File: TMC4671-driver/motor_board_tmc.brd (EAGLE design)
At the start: 60 x 95 mm, 135 parts, among them U1 TMC4671-ES, U10 BSC030N08NS5ATMA1, U11 BSC030N08NS5ATMA1, U12 INA28X, U13 INA28X, U14 BSC030N08NS5ATMA1, U15 BSC030N08NS5ATMA1, U16 BSC030N08NS5ATMA1, U17 BSC030N08NS5ATMA1, U18 MCP14XX, U19 BSC030N08NS5ATMA1, U20 BSC030N08NS5ATMA1, U21 BSC030N08NS5ATMA1, U22 NC7NZ17K8X-3-BUFFER, U23 NC7NZ17K8X-3-BUFFER, U3 LM5109BSD, U4 LM5109BSD, U5 LM5109BSD, U6 LM5109BSD, U7 AP3012KTR-G1, U8 LM5050Q1MK-1/NOPB, U9 BSC030N08NS5ATMA1, X1 GMSTBA4, X2 GMSTBA4, X3 2516-, Y1 ECS-327KE-TR

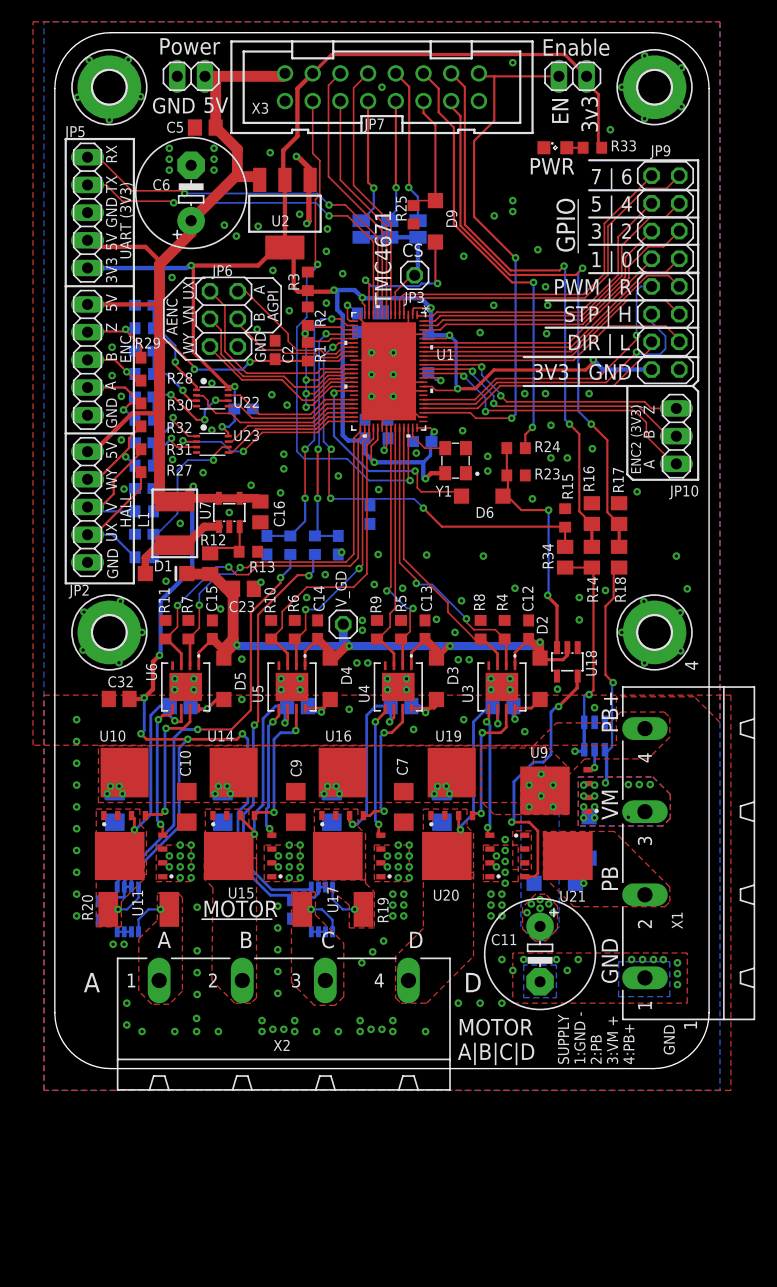
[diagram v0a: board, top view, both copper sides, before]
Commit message: Changing clearances to 8 mil and renamed shunt amps
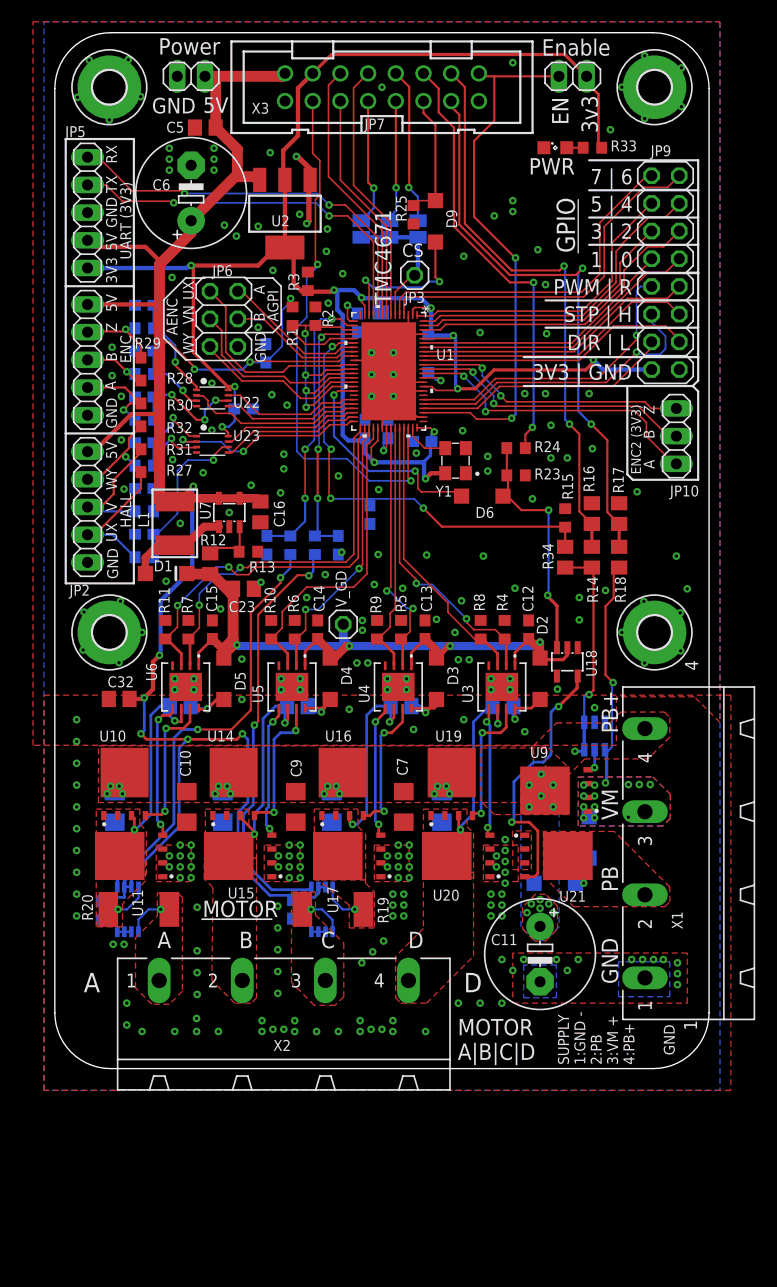
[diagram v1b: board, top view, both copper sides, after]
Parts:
- U12, U13: value INA28X -> AD841X
- moved R1 3.54 mm to (21.8, -26.0), turned to 90 degrees
- moved C2 0.90 mm to (19.4, -29.4), flipped to the bottom
- moved R2 0.70 mm to (23.9, -26.0)
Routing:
- net +5V: track 187.2 -> 195.7 mm, vias 8 -> 9
- net GND: track 41.5 -> 37.5 mm, vias 253 -> 250
- net V_ADC/2: track 33.1 -> 35.3 mm
- net REF_R: track 26.8 -> 25.9 mm

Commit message: Updated TMC4671 board to redesigned 1.2 version.
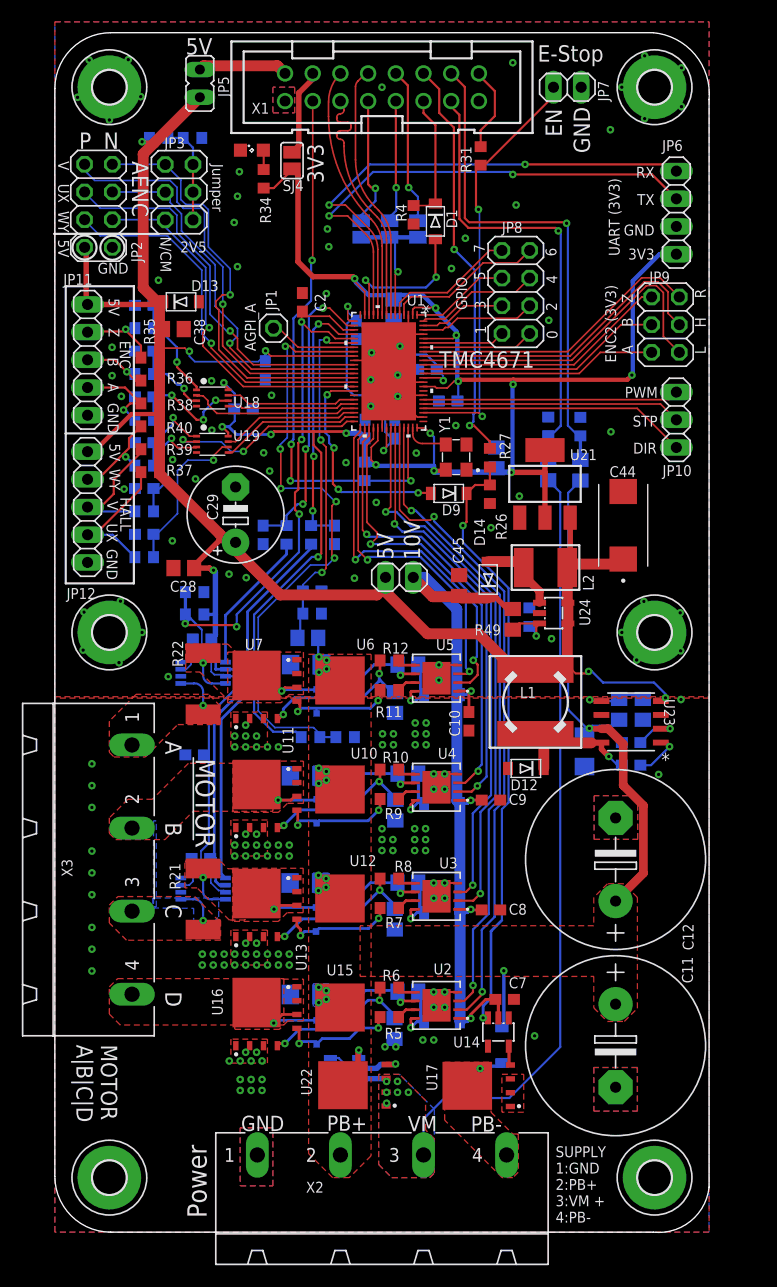
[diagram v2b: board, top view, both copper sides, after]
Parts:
- added C42: 100nF, resistor:C0603
- added C43: 1µF, resistor:C1206
- added C44: 593D476X0016D2TE3, Powermisc:CAPPM7343X310N
- added C45: 4.7µF, resistor:C0805
- added D10: BZX384-XXX, Powermisc:SOD323-R
- added D11: HV >100V, adafruit:SOD-123FL
- added D12, D14: LV low drop, adafruit:SOD-123FL
- added D13: 5.6V zener, adafruit:SOD-123FL
- added H5, H6: MOUNT-PAD-ROUND3.0, holes:3,0-PAD
- added JP11, JP12: (no value), pinhead:1X05
- added L2: 10µH, rcl:L4532P
- added R26, R50: 10k, resistor:R0603
- added R41, R42, R43, R44, R45, R46: 1.5k, resistor:R0603
- added R47: 294k, resistor:R0805
- added R48, R49: 71.5k, resistor:R0805
- added SJ4: 3.3V, jumper:SJ
- added U24: AP3012KTR-G1, Powermisc:SOT23-5L
- C10, C17, C18, C19, C7, C9: value 1µF -> 100nF; device resistor:C1206 -> resistor:C0603
- C11: value 100µF+ -> 680µF; device resistor:E5-10,5 -> resistor:E7,5-16
- C12: value 100nF -> 680µF; device resistor:C0603 -> resistor:E7,5-16
- C13, C14, C15: value 100nF -> 1µF; device resistor:C0603 -> resistor:C1206
- C16: value 4.7µF -> 1µF; device resistor:C0805 -> resistor:C1206
- C20: value 1µF -> 4.7µF; device resistor:C1206 -> resistor:C0805
- C21, C22, C24: device resistor:C0603 -> resistor:C0805
- C23: value 4.7µF -> 100nF
- C25, C30, C31: value 100nF -> 1n
- C26, C27: device resistor:C0805 -> resistor:C0603
- C28: value 100nF -> 4.7µF
- C29: value 100nF -> (none); device resistor:C0805 -> resistor:E5-8,5
- C32: value 4.7µF -> 100p; device resistor:C0805 -> resistor:C0603
- C33, C35, C37: value 2.2n -> 1n
- C34, C36: value 2.2n -> 100p
- C38, C40: value 2.2n -> 4.7µF; device resistor:C0603 -> resistor:C0805
- C39: value 2.2n -> 100nF; device resistor:C0603 -> resistor:C0805
- C41: value 2.2n -> 100nF
- C5, C8: value 4.7µF -> 100nF; device resistor:C0805 -> resistor:C0603
- C6: value 60µF+ -> 100nF; device resistor:E5-10,5 -> resistor:C0603
- D1, D2, D3, D4, D5: device diode:SOD123 -> adafruit:SOD-123FL
- D6: value LV low drop -> BZX384-XXX; device diode:SOD123 -> Powermisc:SOD323-R
- D7, D8: value HV >100V -> BZX384-XXX; device diode:SOD123 -> Powermisc:SOD323-R
- D9: value HV >100V -> LV low drop; device diode:SOD123 -> adafruit:SOD-123FL
- JP1: device pinhead:1X05 -> pinhead:1X01
- JP2: device pinhead:1X05 -> pinhead:2X04
- JP3: device pinhead:1X01 -> pinhead:2X03
- JP4: device pinhead:1X01 -> pinhead:1X02
- JP5: value (none) -> 5V; device pinhead:1X05 -> jumper:JP1
- JP6: device pinhead:2X03 -> pinhead:1X04
- JP8: device pinhead:1X02 -> pinhead:2X04
- JP9: device pinhead:2X08 -> pinhead:2X03
- L1: value 10µH -> 220µH; device rcl:L4532P -> Powermisc:8MMINDUCTOR
- LED1: value (none) -> Green
- R10, R11, R5, R6, R7, R8, R9: value 10k -> 2.2
- R12: value 33k -> 2.2; device resistor:R0805 -> resistor:R0603
- R13: value 4.7k -> 71.5k; device resistor:R0603 -> resistor:R0805
- R14: value 976k -> 1.5k; device resistor:R0805 -> resistor:R0603
- R15: value 4.7k -> 294k; device resistor:R0603 -> resistor:R0805
- R16: value 33k -> 10k; device resistor:R0805 -> resistor:R0603
- R17: value 976k -> 33k
- R18: value 33k -> 294k
- R19: value 1.5m -> 10k; device resistor:R2512 -> resistor:R0603
- R20: value 1.5m -> 33k; device resistor:R2512 -> resistor:R0805
- R21, R22: value 1k -> 1.5m; device resistor:R0603 -> resistor:R2512
- R23: value 10k -> 1.5k
- R24: value 1k -> 1.5k
- R25: value 10k -> 33k; device resistor:R0603 -> resistor:R0805
- R27, R30, R31: value 4.7k -> 1.5k
- R28: value 4.7k -> 33k; device resistor:R0603 -> resistor:R0805
- R29: value 4.7k -> 22k thermistor
- R32: value 4.7k -> 10k
- R33: value 330 -> 10k
- R34: value 360k -> 330; device resistor:R0805 -> resistor:R0603
- R35, R36, R37, R38, R39, R40: value 1k -> 4.7k
- U1: value TMC4671-ES -> TMC4671
- U12, U13: value AD841X -> BSC030N08NS5ATMA1; device Powermisc:MSOP8 -> OHSC_Power:MOSFET_BSC093N04LSGATMA1
- U14: value BSC030N08NS5ATMA1 -> MCP14XX; device OHSC_Power:MOSFET_BSC093N04LSGATMA1 -> Powermisc:SOT23-5L
- U18: value MCP14XX -> NC7NZ17K8X-3-BUFFER; device Powermisc:SOT23-5L -> Powermisc:VFSOP-8
- U19: value BSC030N08NS5ATMA1 -> NC7NZ17K8X-3-BUFFER; device OHSC_Power:MOSFET_BSC093N04LSGATMA1 -> Powermisc:VFSOP-8
- U2: value (none) -> LM5109BSD; device SparkFun-IC-Power:SOT223 -> Powermisc:SDC08A
- U20: value BSC030N08NS5ATMA1 -> LM74700-Q1; device OHSC_Power:MOSFET_BSC093N04LSGATMA1 -> OHSC_Power:SOT23-6
- U21: value BSC030N08NS5ATMA1 -> (none); device OHSC_Power:MOSFET_BSC093N04LSGATMA1 -> SparkFun-IC-Power:SOT223
- U22: value NC7NZ17K8X-3-BUFFER -> BSC030N08NS5ATMA1; device Powermisc:VFSOP-8 -> OHSC_Power:MOSFET_BSC093N04LSGATMA1
- U23: value NC7NZ17K8X-3-BUFFER -> MAX5033BASA+T; device Powermisc:VFSOP-8 -> Powermisc:21-0041B_8_MXM
- U6: value LM5109BSD -> BSC030N08NS5ATMA1; device Powermisc:SDC08A -> OHSC_Power:MOSFET_BSC093N04LSGATMA1
- U7: value AP3012KTR-G1 -> BSC030N08NS5ATMA1; device Powermisc:SOT23-5L -> OHSC_Power:MOSFET_BSC093N04LSGATMA1
- U8: value LM5050Q1MK-1/NOPB -> AD841X; device OHSC_Power:SOT95P280X110-6N -> Powermisc:MSOP8
- U9: value BSC030N08NS5ATMA1 -> AD841X; device OHSC_Power:MOSFET_BSC093N04LSGATMA1 -> Powermisc:MSOP8
- X1: value GMSTBA4 -> 2516-; device con-phoenix-762:GMSTBA4 -> con-3m:PAK100/2500-16
- X3: value 2516- -> GMSTBA4; device con-3m:PAK100/2500-16 -> con-phoenix-762:GMSTBA4
- Y1: value ECS-327KE-TR -> 25MHz
- moved H1 100.0 mm to (55.0, -105.0)
- moved X3 77.0 mm to (2.00, -76.8), turned to 270 degrees
- moved X1 76.1 mm to (30.0, -5.00), turned to 0 degrees
- moved U2 73.9 mm to (35.0, -89.2), turned to 90 degrees
- moved C39 71.1 mm to (26.2, -98.0)
- moved H2 70.7 mm to (5.00, -105.0)
- moved R25 64.6 mm to (31.2, -81.3), flipped to the bottom
- moved U22 64.4 mm to (27.5, -96.5), turned to 90 degrees
- moved R28 63.5 mm to (31.1, -91.3), flipped to the bottom, turned to 90 degrees
- moved C21 60.3 mm to (32.4, -88.0)
- moved C8 54.8 mm to (40.0, -80.5), flipped to the top, turned to 180 degrees
- moved C41 54.8 mm to (52.9, -65.1)
- moved H3 50.0 mm to (55.0, -5.00)
- moved H4 50.0 mm to (55.0, -55.0)
- moved R19 48.5 mm to (45.2, -36.1), flipped to the bottom, turned to 270 degrees
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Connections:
- removed net N$14: C28.1, D4.C, U5.8
- removed net N$26: C26.1, D2.C, U3.8
- removed net VCORE1: C3.2, U1.15
- removed net VCORE2: C1.2, U1.45
- removed net VCORE3: C4.2, U1.63
- removed net V_ADC/2: R1.1, R2.2, U1.17, U1.19, U1.26, U1.28, U1.30
- new net AENC_UX_N: JP2.5, JP3.3, U1.26
- new net AENC_VN_N: JP2.7, JP3.1, U1.28
- new net AENC_WY_N: JP2.3, JP3.5, U1.30
- new net INPUT_GATE: U20.5, U22.4
- new net N$16: C42.2, D12.C, L1.1, U23.8
- new net N$17: R31.2, X1.16
- new net N$19: C42.1, U23.1
- new net N$20: SJ4.1, X1.4
- new net N$21: R47.1, R48.1, U23.5
- new net N$23: JP5.1, X1.2
- new net N$24: C39.1, U20.1
- new net N$25: C41.2, U23.2
- new net N$27: R11.2, U5.7
- new net N$28: C23.1, D4.C, U4.8
- new net N$29: R10.2, U4.5
- new net N$30: R9.2, U4.7
- new net N$31: C21.1, D2.C, U2.8
- new net N$32: R6.2, U2.5
- new net N$33: R5.2, U2.7
- new net N$34: C22.1, D3.C, U3.8
- new net N$35: R8.2, U3.5
- new net N$36: R7.2, U3.7
- new net VCORE: C3.2, C5.2, C6.2, U1.15, U1.45, U1.63
- new net V_SENSE/2: C1.2, C2.2, R1.1, R2.2, U1.17, U1.19, U8.3, U8.7, U9.3, U9.7
- net +3V3: now also C17.1, C18.1, C19.1, C20.1, C40.1, JP6.4, R29.2, R34.2, SJ4.2, U18.P$8, U19.P$8, U21.2, U21.4; no longer C21.1, C22.1, C24.1, C25.1, C8.1, JP5.5, JP7.2, JP9.2, R33.2, U2.2, U2.4, U22.P$8, U23.P$8, X3.4
- net +5V: now also C26.1, C27.1, C28.1, C29.+, C38.1, C4.2, C44.1, D13.C, JP11.1, JP12.1, JP2.2, JP4.2, JP5.2, L1.2, L2.1, R35.2, R36.2, R37.2, R38.2, R39.2, R40.2, U21.3, U23.4, U24.4, U24.5, U8.6, U9.6; no longer C16.1, C2.2, C30.1, C31.1, C32.1, C5.1, C6.+, JP1.1, JP2.1, JP5.4, JP8.1, L1.1, R27.2, R28.2, R29.2, R30.2, R31.2, U12.6, U12.7, U13.6, U13.7, U2.3, U7.4, U7.5, X3.2
- net AENC_UX: now also JP2.6; no longer JP6.1
- net AENC_VN: now also JP2.8; no longer JP6.3
- net AENC_WY: now also JP2.4; no longer JP6.5
- net AGPI_A: now also JP1.1; no longer JP6.2
- net AGPI_B: now also R29.1, R30.2; no longer JP6.4
- net BRAKE_CTRL: now also D9.C, R26.2, R27.2, U14.3; no longer D6.C, R23.2, R24.2, U18.3
- net BRAKE_CTRL_EXT: now also R27.1, X1.12; no longer R24.1, X3.12
- net BRAKE_CTRL_TMC: now also D9.A; no longer D6.A
- net BRAKE_GATE: now also U14.5, U17.4; no longer U18.5, U21.4
- net CS1: now also X1.7; no longer X3.7
- net CS2: now also X1.9; no longer X3.9
- net CS3: now also X1.10; no longer X3.10
- net CS_TMC: no longer JP3.1
- net C_HS_A: now also U5.2; no longer R7.2, U6.2
- net C_HS_B: now also U4.2; no longer R6.2, U5.2
- net C_HS_C: now also U3.2; no longer R5.2, U4.2
- net C_HS_D: now also U2.2; no longer R4.2, U3.2
- net C_LS_A: now also U5.3; no longer R11.2, U6.3
- net C_LS_B: now also U4.3; no longer R10.2, U5.3
- net C_LS_C: now also U3.3; no longer R9.2, U4.3
- net C_LS_D: now also U2.3; no longer R8.2, U3.3
- net DIR: now also JP10.3; no longer JP9.4
- net ENABLE: now also JP7.2, R31.1; no longer JP7.1, X3.16
- net ENC2_A: now also JP9.2; no longer JP10.1
- net ENC2_B: now also JP9.4; no longer JP10.2
- net ENC2_Z: now also JP9.6; no longer JP10.3
- net ENC_A: now also U18.P$2; no longer U22.P$2
- net ENC_A_5V: now also C36.2, R46.1, U18.P$6; no longer C41.2, R40.1, U22.P$6
- net ENC_B: now also U18.P$5; no longer U22.P$5
- net ENC_B_5V: now also C34.2, R45.1, U18.P$3; no longer C39.2, R39.1, U22.P$3
- net ENC_Z: now also U18.P$7; no longer U22.P$7
- net ENC_Z_5V: now also C32.2, R44.1, U18.P$1; no longer C40.2, R38.1, U22.P$1
- net FLAG: now also D1.C, R4.2, X1.11; no longer D9.C, R25.2, X3.11
- net GND: now also C10.1, C12.-, C13.2, C14.2, C15.2, C26.2, C27.2, C28.2, C29.-, C30.1, C31.1, C32.1, C33.1, C38.2, C40.2, C43.1, C44.2, C45.2, C5.1, C6.1, C7.1, C8.1, C9.1, D12.A, D13.A, H5.B3,0, H6.B3,0, JP11.5, JP12.5, JP2.1, JP6.3, JP7.1, R14.1, R17.1, R19.1, R20.1, R26.1, R28.1, R30.1, R33.1, R48.2, R50.1, U13.1, U14.1, U14.4, U16.1, U16.2, U16.3, U18.P$4, U19.P$4, U2.4, U2.9, U23.3, U23.6, U24.2, U7.1, U7.3, U9.2, X2.1; no longer C10.2, C12.1, C13.1, C14.1, C15.1, C21.2, C22.2, C23.2, C24.2, C30.2, C31.2, C32.2, C33.2, C38.1, C39.1, C40.1, C5.2, C6.-, C7.2, C8.2, C9.2, D8.A, JP1.5, JP2.5, JP5.3, JP6.6, JP8.2, JP9.1, R10.1, R11.1, R13.1, R15.1, R18.1, R23.1, R5.1, R6.1, R7.1, R8.1, R9.1, U12.2, U12.3, U12.4, U13.4, U15.1, U15.2, U15.3, U18.1, U18.4, U2.1, U20.1, U20.3, U21.2, U21.3, U22.P$4, U23.P$4, U6.4, U6.9, U8.3, X3.1
- net GPIO0: now also JP8.1; no longer JP9.9
- net GPIO1: now also JP8.2; no longer JP9.10
- net GPIO2: now also JP8.3; no longer JP9.11
- net GPIO3: now also JP8.4; no longer JP9.12
- net GPIO4: now also JP8.5; no longer JP9.13
- net GPIO5: now also JP8.6; no longer JP9.14
- net GPIO6: now also JP8.7; no longer JP9.15
- net GPIO7: now also JP8.8; no longer JP9.16
- net G_HS_A: now also D6.C, R11.1, U6.4; no longer U10.4, U6.7
- net G_HS_B: now also D7.C, R9.1, U10.4; no longer U14.4, U5.7
- net G_HS_C: now also D8.C, R7.1, U12.4; no longer U16.4, U4.7
- net G_HS_D: now also D10.C, R5.1, U15.4; no longer U19.4, U3.7
- net G_LS_A: now also R12.1, R17.2, U7.4; no longer U11.4, U6.5
- net G_LS_B: now also R10.1, R20.2, U11.4; no longer U15.4, U5.5
- net G_LS_C: now also R25.2, R8.1, U13.4; no longer U17.4, U4.5
- net G_LS_D: now also R28.2, R6.1, U16.4; no longer U20.4, U3.5
- net HALL_UX: now also U19.P$2; no longer U23.P$2
- net HALL_UX_5V: now also C33.2, R41.1, U19.P$6; no longer C37.2, R35.1, U23.P$6
- net HALL_V: now also U19.P$5; no longer U23.P$5
- net HALL_V_5V: now also C35.2, R42.1, U19.P$3; no longer C36.2, R36.1, U23.P$3
- net HALL_WY: now also U19.P$7; no longer U23.P$7
- net HALL_WY_5V: now also C37.2, R43.1, U19.P$1; no longer C38.2, R37.1, U23.P$1
- net MISO: now also X1.6; no longer X3.6
- net MOSI: now also X1.5; no longer X3.5
- net MOT_A: now also C24.2, D6.A, R22.2, U5.6, U6.1, U6.2, U6.3, U7.5, U8.8; no longer C29.2, R20.2, U10.1, U10.2, U10.3, U11.5, U12.8, U6.6
- net MOT_A_OUT: now also R22.1, U8.1, X3.1; no longer R20.1, U12.1, X2.1
- net MOT_B: now also C23.2, D7.A, U10.1, U10.2, U10.3, U11.5, U4.6, X3.2; no longer C28.2, U14.1, U14.2, U14.3, U15.5, U5.6, X2.2
- net MOT_C: now also C22.2, D8.A, R21.2, U12.1, U12.2, U12.3, U13.5, U3.6, U9.8; no longer C27.2, R19.2, U13.8, U16.1, U16.2, U16.3, U17.5, U4.6
- net MOT_C_OUT: now also R21.1, U9.1, X3.3; no longer R19.1, U13.1, X2.3
- net MOT_D: now also C21.2, D10.A, U15.1, U15.2, U15.3, U16.5, U2.6, X3.4; no longer C26.2, U19.1, U19.2, U19.3, U20.5, U3.6, X2.4
- net N$1: now also JP12.4, R37.1, R41.2; no longer JP2.4, R27.1, R35.2
- net N$10: now also R24.2, U9.5; no longer R22.2, U13.5
- net N$11: now also JP11.2, R35.1, R44.2; no longer JP1.2, R29.1, R38.2
- net N$12: now also D14.A, L2.2, U24.1; no longer D1.A, L1.2, U7.1
- net N$13: now also R12.2, U5.5; no longer U8.5, U9.4
- net N$15: now also JP12.2, R40.1, R43.2; no longer JP2.2, R32.1, R37.2
- net N$18: now also C24.1, U5.8; no longer C29.1, U6.8
- net N$2: now also X1.15; no longer X3.15
- net N$22: now also JP3.2, JP3.4, JP3.6, R32.1, R33.2; no longer C27.1, D3.C, U4.8
- net N$3: now also JP12.3, R39.1, R42.2; no longer JP2.3, R31.1, R36.2
- net N$4: now also D1.A; no longer D9.A
- net N$5: now also R49.1, R50.2, U24.3; no longer R12.1, R13.2, U7.3
- net N$6: now also R23.2, U8.5; no longer R21.2, U12.5
- net N$7: now also JP11.4, R38.1, R46.2; no longer JP1.4, R30.1, R40.2
- net N$8: now also R34.1; no longer R33.1
- net N$9: now also JP11.3, R36.1, R45.2; no longer JP1.3, R28.1, R39.2
- net PWM_I: now also JP10.1; no longer JP9.8
- net REF_H: now also JP9.3; no longer JP9.5
- net REF_L: now also JP9.1; no longer JP9.3
- net REF_R: now also JP9.5; no longer JP9.7
- net RESET: now also X1.3; no longer X3.3
- net RES_FET: now also D11.A, U17.5, X2.4; no longer D7.A, U21.5, X1.2
- net SCK: now also X1.8; no longer X3.8
- net SENSE_A: now also C30.2, R23.1; no longer C34.2, R21.1
- net SENSE_C: now also C31.2, R24.1; no longer C35.2, R22.1
- net STEP: now also JP10.2; no longer JP9.6
- net UART_RX: now also JP6.1; no longer JP5.1
- net UART_TX: now also JP6.2; no longer JP5.2
- net V+: now also C12.+, C13.1, C14.1, C15.1, C16.1, C43.2, D11.C, R13.2, R15.2, R47.2, U12.5, U15.5, U20.4, U22.5, U23.7, U6.5, X2.2; no longer C10.1, C17.1, C18.1, C19.1, C20.1, C7.1, C9.1, D7.C, R14.2, R34.2, U14.5, U16.5, U19.5, U8.1, U8.6, U9.5, X1.4
- net V_EXT: now also R18.1, R19.2, X1.13; no longer R17.1, R18.2, X3.13
- net V_GD: now also C10.2, C45.1, C7.2, C8.2, C9.2, D14.C, R49.2, U14.2, U2.1; no longer C12.2, C13.2, C14.2, C15.2, C23.1, D1.C, R12.2, U18.2, U6.1
- net V_INT: now also R15.1, X1.14; no longer R14.1, X3.14
- net V_INT_TMC: now also C25.1, R13.1, R14.2; no longer C33.1, R15.2, R34.1
- net V_MOT_IN: now also C39.2, R18.2, U20.3, U20.6, U22.1, U22.2, U22.3, X2.3; no longer D8.C, R17.2, U8.4, U9.1, U9.2, U9.3, X1.3
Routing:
- net V_SENSE/2: track 0.00 -> 87.8 mm, vias 0 -> 5
- net V_MOT_IN: track 21.1 -> 80.2 mm, vias 14 -> 6
- net AGPI_B: track 12.4 -> 57.1 mm, vias 0 -> 5
- net AENC_VN_N: track 0.00 -> 39.8 mm, vias 0 -> 1
- net V+: track 20.7 -> 59.6 mm, vias 30 -> 19
- net V_ADC/2: track 35.3 -> 0.00 mm, vias 4 -> 0
- net VCORE: track 0.00 -> 34.5 mm, vias 0 -> 3
- net AENC_UX_N: track 0.00 -> 34.4 mm, vias 0 -> 1
- net AENC_WY_N: track 0.00 -> 33.9 mm, vias 0 -> 1
- net C_HS_D: track 27.9 -> 61.4 mm
- net BRAKE_CTRL: track 22.2 -> 55.5 mm
- net C_LS_D: track 26.1 -> 58.5 mm, vias 0 -> 2
- net C_HS_C: track 24.1 -> 51.3 mm
- net N$6: track 39.7 -> 13.1 mm, vias 2 -> 0
- net C_LS_C: track 23.4 -> 49.1 mm, vias 0 -> 2
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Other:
- board size 60 x 95 mm -> 60 x 110 mm
- board text added: "0"
- board text added: "10V"
- board text added: "2V5"
- board text added: "5"
- board text added: "6"
- board text added: "7"
- board text added: "AGPI_A"
- board text added: "Cos"
- board text added: "DIR"
- board text added: "E-Stop"
- board text added: "H"
- board text added: "Jumper"
- board text added: "L"
- board text added: "N"
- board text added: "N/CM"
- board text added: "P"
- board text added: "PB-"
- board text added: "PWM"
- board text added: "SE Select"
- board text added: "STP"
- board text added: "SUPPLY 1:GND 2:PB+ 3:VM + 4:PB-"
- board text added: "Sin"
- board text added: "Supply: PSU (protected): use VM (+) and GND (-) ALWAYS use braking resistor between PB+ and PB Battery (unprotected. regen. braking): Only PB+ (+) and GND (-)"
- board text added: "TMP"
- board text added: "V1.2 - YR 2020"
- board text removed: "0|2|4|6 1|3|5|7"
- board text removed: "1 | 0"
- board text removed: "1mm lower"
- board text removed: "3 | 2"
- board text removed: "3V3 | GND"
- board text removed: "3v3"
- board text removed: "5 | 4"
- board text removed: "7 | 6"
- board text removed: "AGPI"
- board text removed: "Bigger cap! (470µF+) External headers"
- board text removed: "CS"
- board text removed: "DBGSPI: 3:CS 4:SCK 5:MOSI 6:MISO 7:TRG"
- board text removed: "DIR | L"
- board text removed: "DIR|STP|PWM"
- board text removed: "Enable"
- board text removed: "Ensure good GND for motor supply"
- board text removed: "GND 3V3"
- board text removed: "PB"
- board text removed: "PWM | R"
- board text removed: "PWR"
- board text removed: "REF(L,H,R)"
- board text removed: "STP | H"
- board text removed: "SUPPLY 1:GND - 2:PB 3:VM + 4:PB+"
- board text removed: "Status pin parallel Filter v-sense?"
- board text removed: "Supply: PSU (protected): use VM (+) and GND (-) Must use braking resistor between PB+ and PB Battery (allow backfeed): Only PB+ and GND"
- board text removed: "V1.1 YR 2020"
- board text removed: "VN"
- board text removed: "V_GD"

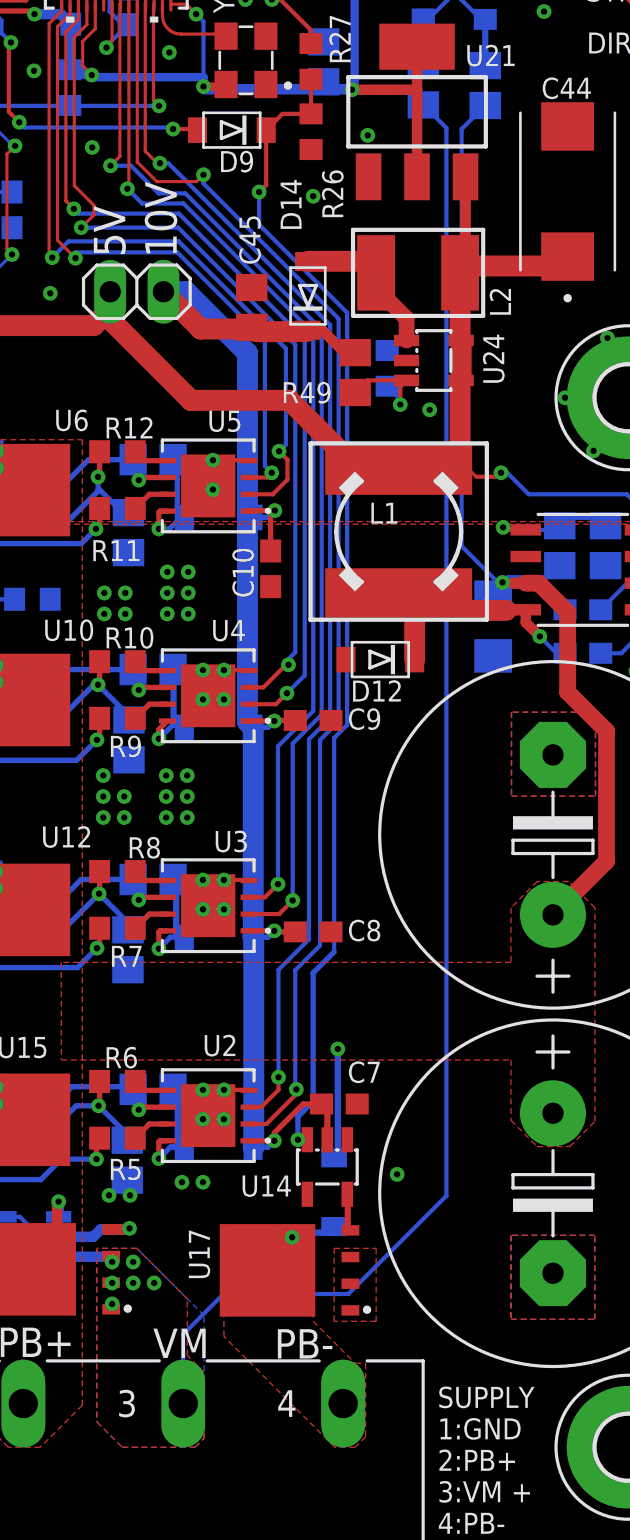
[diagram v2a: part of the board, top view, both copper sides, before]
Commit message: Updated TMC Board. Fixed D12 value
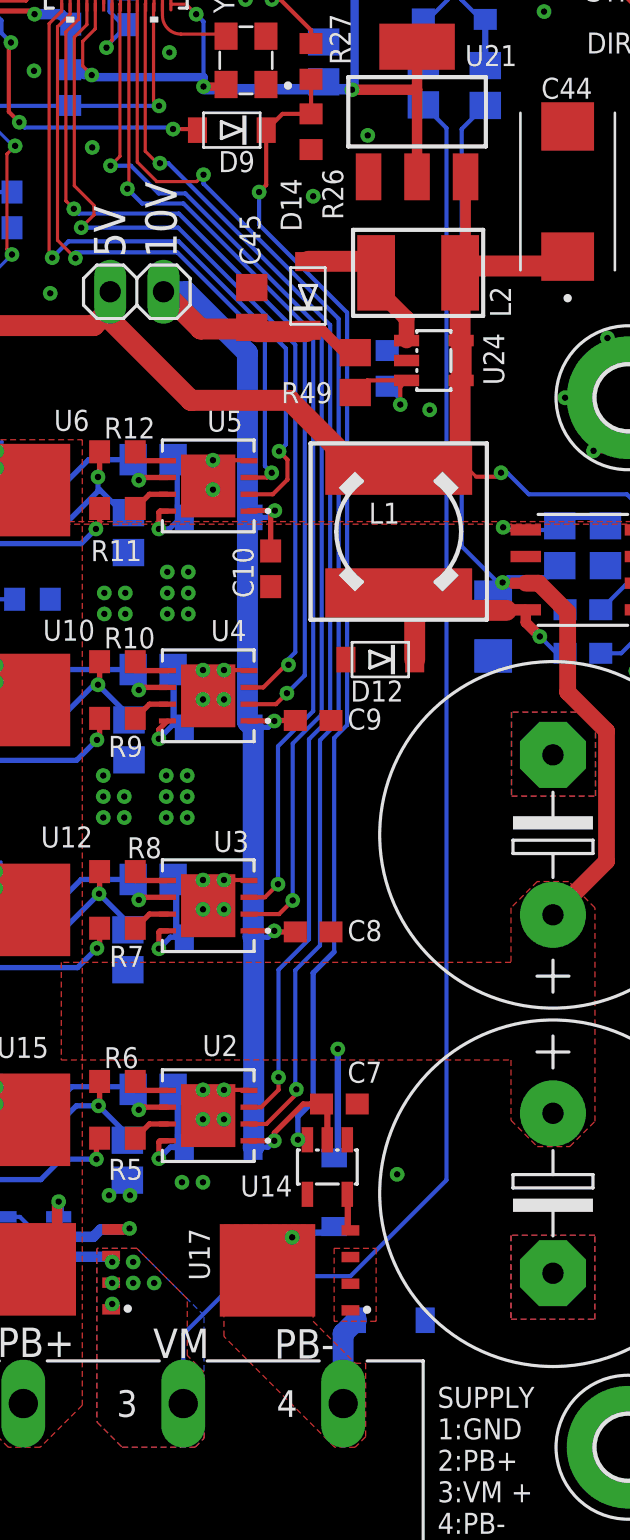
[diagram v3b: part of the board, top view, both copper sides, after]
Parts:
- added D15: Zener 65V, adafruit:SOD-123FL
- D12: value LV low drop -> HV >100V
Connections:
- net GND: now also D15.A
- net RES_FET: now also D15.C
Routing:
- net RES_FET: track 4.44 -> 8.67 mm
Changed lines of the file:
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@@
 <layer number="45" name="Holes" color="7" fill="1" visible="no" active="yes"/>
 <layer number="46" name="Milling" color="3" fill="1" visible="no" active="yes"/>
-<layer number="47" name="Measures" color="7" fill="1" visible="no" active="yes"/>
-<layer number="48" name="Document" color="7" fill="1" visible="no" active="yes"/>
-<layer number="49" name="Reference" color="7" fill="1" visible="no" active="yes"/>
+<layer number="47" name="Measures" color="7" fill="1" visible="yes" active="yes"/>
+<layer number="48" name="Document" color="7" fill="1" visible="yes" active="yes"/>
+<layer number="49" name="Reference" color="7" fill="1" visible="yes" active="yes"/>
 <layer number="50" name="dxf" color="7" fill="1" visible="no" active="no"/>
 <layer number="51" name="tDocu" color="7" fill="1" visible="yes" active="yes"/>
@@
 <text x="12.2" y="-0.5" size="1.4224" layer="22" font="vector" rot="SMR180">5V</text>
 <wire x1="9.9" y1="-36.6" x2="11.9" y2="-36.6" width="0.2" layer="22"/>
-<wire x1="-32.45" y1="-44.475" x2="-32.45" y2="-94.475" width="0.254" layer="49"/>
-<wire x1="-32.45" y1="-44.475" x2="-60.45" y2="-44.475" width="0.254" layer="49"/>
+<wire x1="-18.45" y1="-56.475" x2="-18.45" y2="-106.475" width="0.254" layer="49"/>
+<wire x1="-18.45" y1="-56.475" x2="-46.45" y2="-56.475" width="0.254" layer="49"/>
 <text x="7.075" y="-11.775" size="1.5" layer="21" font="vector" rot="SR270">AENC</text>
 <text x="2.225" y="-10.65" size="1.5" layer="21" font="vector">P</text>
@@
 <circle x="2.725" y="-19.7" radius="1.101134375" width="0.2" layer="22"/>
 <circle x="5.275" y="-19.725" radius="1.101134375" width="0.2" layer="22"/>
-<text x="44.3" y="-107.1" size="2" layer="22" font="vector" rot="MR90">Power</text>
+<text x="43.825" y="-107.625" size="2" layer="22" font="vector" rot="MR90">Power</text>
 <text x="31.05" y="-48.3" size="1.5" layer="21" font="vector" rot="R90">5V</text>
 <text x="30.875" y="-51.7" size="1.5" layer="22" font="vector" rot="MR270">5V</text>
@@
 <attribute name="VALUE" x="40.955" y="-11.935" size="1.27" layer="27" rot="R90"/>
 </element>
-<element name="D12" library="adafruit" library_urn="urn:adsk.eagle:library:420" package="SOD-123FL" package3d_urn="urn:adsk.eagle:package:6240937/1" value="LV low drop" x="43.2" y="-67.475" locked="yes" smashed="yes" rot="R180">
+<element name="D12" library="adafruit" library_urn="urn:adsk.eagle:library:420" package="SOD-123FL" package3d_urn="urn:adsk.eagle:package:6240937/1" value="HV &gt;100V" x="43.2" y="-67.475" locked="yes" smashed="yes" rot="R180">
 <attribute name="NAME" x="44.3" y="-68.475" size="1" layer="25" font="vector" rot="R180"/>
 <attribute name="VALUE" x="44.3" y="-65.175" size="1.27" layer="27" rot="R180"/>
@@
 <attribute name="NAME" x="14.96399375" y="-44.709803125" size="1" layer="25" font="vector" ratio="10" rot="R90"/>
 <attribute name="VALUE" x="19.59759375" y="-46.7146" size="1.27" layer="27" ratio="10" rot="R90"/>
+</element>
+<element name="D15" library="adafruit" library_urn="urn:adsk.eagle:library:420" package="SOD-123FL" package3d_urn="urn:adsk.eagle:package:6240937/1" value="Zener 65V" x="43.7" y="-98.95" smashed="yes" rot="MR180">
+<attribute name="NAME" x="45.2" y="-97.825" size="1" layer="26" rot="MR0"/>
+<attribute name="VALUE" x="42.6" y="-97.666" size="0.4064" layer="28" rot="MR180"/>
 </element>
 </elements>
@@
 <contactref element="C29" pad="-"/>
 <via x="44" y="-92" extent="1-16" drill="0.3"/>
+<contactref element="D15" pad="A"/>
 </signal>
 <signal name="G_LS_D">
@@
 <wire x1="30.425" y1="-96.175" x2="30.175" y2="-95.925" width="0.5" layer="16"/>
 <wire x1="30.175" y1="-95.925" x2="27.875" y2="-95.925" width="0.5" layer="16"/>
-<wire x1="46.35" y1="-93.025" x2="46.35" y2="-42.15" width="0.2" layer="16"/>
-<wire x1="35.73" y1="-97.7" x2="33.81" y2="-99.62" width="0.2" layer="16"/>
+<wire x1="46.35" y1="-92.275" x2="46.35" y2="-42.15" width="0.2" layer="16"/>
+<wire x1="36.58" y1="-96.85" x2="33.81" y2="-99.62" width="0.2" layer="16"/>
 <wire x1="33.81" y1="-102.92" x2="33.81" y2="-99.62" width="0.2" layer="16"/>
-<wire x1="35.73" y1="-97.7" x2="41.675" y2="-97.7" width="0.2" layer="16"/>
-<wire x1="41.675" y1="-97.7" x2="46.35" y2="-93.025" width="0.2" layer="16"/>
+<wire x1="36.58" y1="-96.85" x2="41.775" y2="-96.85" width="0.2" layer="16"/>
+<wire x1="41.775" y1="-96.85" x2="46.35" y2="-92.275" width="0.2" layer="16"/>
 <wire x1="46.35" y1="-42.15" x2="45.25" y2="-41.05" width="0.2" layer="16"/>
 <wire x1="25.275" y1="-94.025" x2="26.025" y2="-94.025" width="0.2" layer="16"/>
@@
 <wire x1="39" y1="-95" x2="37.825" y2="-96.175" width="0.254" layer="1"/>
 <wire x1="37.825" y1="-96.175" x2="37.825" y2="-96.575" width="0.254" layer="1"/>
+<contactref element="D15" pad="C"/>
+<wire x1="42.0625" y1="-98.95" x2="41.43" y2="-99.5825" width="1" layer="16"/>
+<wire x1="41.43" y1="-99.5825" x2="41.43" y2="-102.92" width="1" layer="16"/>
 </signal>
 <signal name="MOSI">
